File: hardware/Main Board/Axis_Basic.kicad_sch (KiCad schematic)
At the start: 63 parts, among them J1 USB4105-GF-A, J2 JST_PH, J3 JST_PH, J4 S2B-PH-K-S, J5 1175-1628-ND, J6 1-84952-4, SW1 RKB2SJK, SW2 RKB2SJK, U1 TLV493D, U2 UA78M33CDCYR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

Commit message: missed connections
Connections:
- net User_Input: now also U3.32 (PA15)
- no-connect marks 22 -> 21
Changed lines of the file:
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@@
-	)
-	(no_connect
-		(at 140.335 126.365)
 	)
 	(no_connect
@@
 			(effects
 				(font
+					(size 1.27 1.27)
+				)
+				(justify left)
+				(hide yes)
+			)
+		)
+	)
+	(global_label "User_Input"
+		(shape input)
+		(at 140.335 126.365 0)
+		(fields_autoplaced yes)
+		(effects
+			(font
+				(size 1.27 1.27)
+			)
+			(justify left)
+		)
+		(property "Intersheetrefs" "${INTERSHEET_REFS}"
+			(at 153.2987 126.365 0)
+			(effects
+				(font

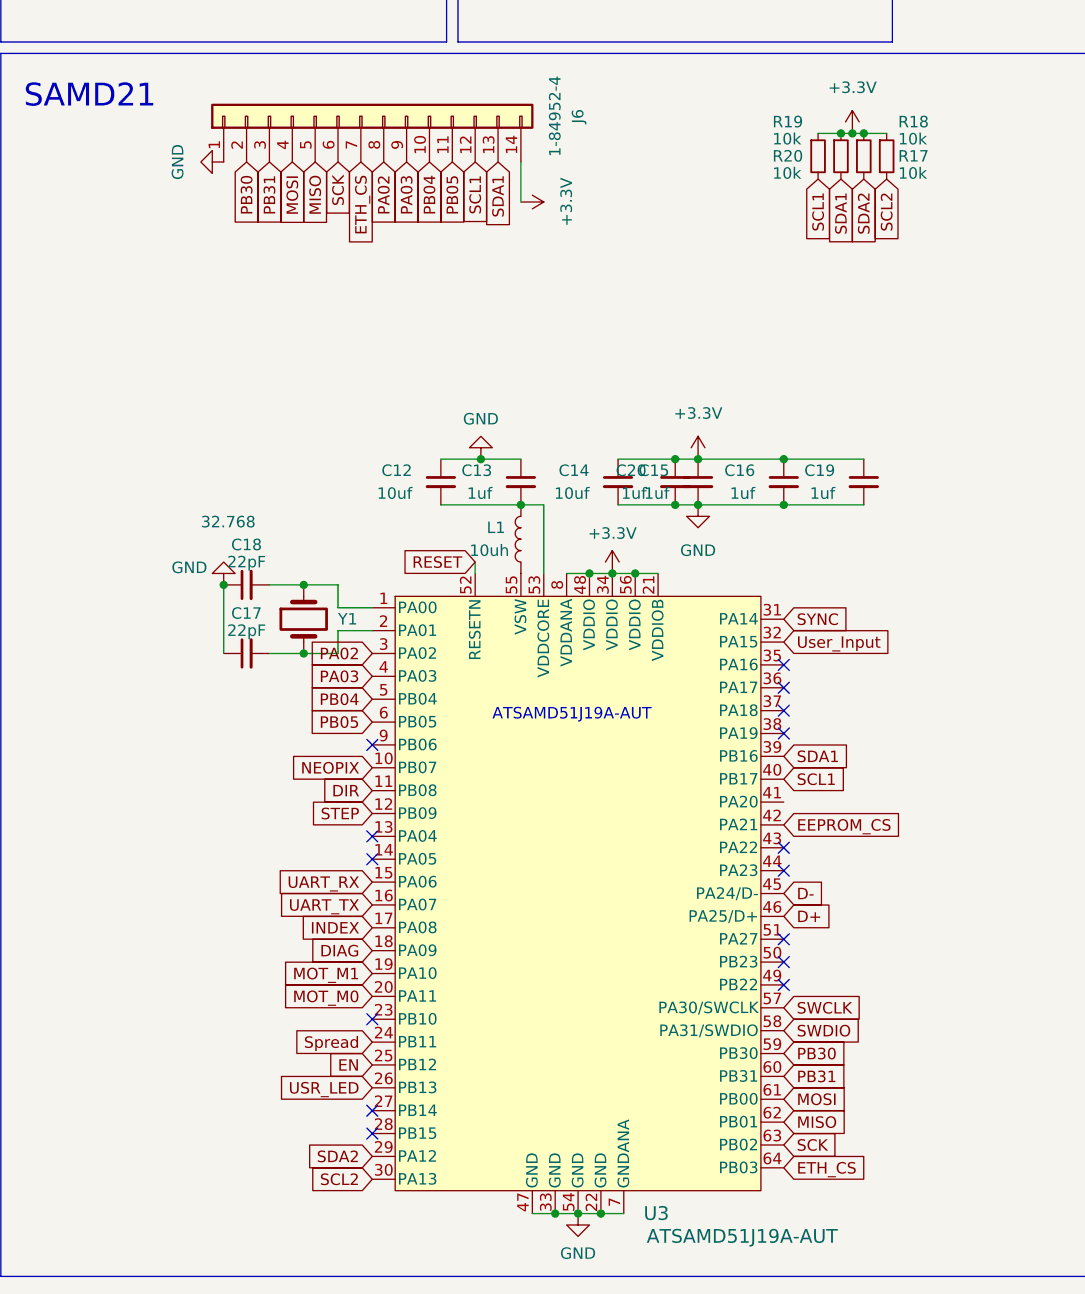
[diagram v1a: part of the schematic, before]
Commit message: Move pins for addressable LED
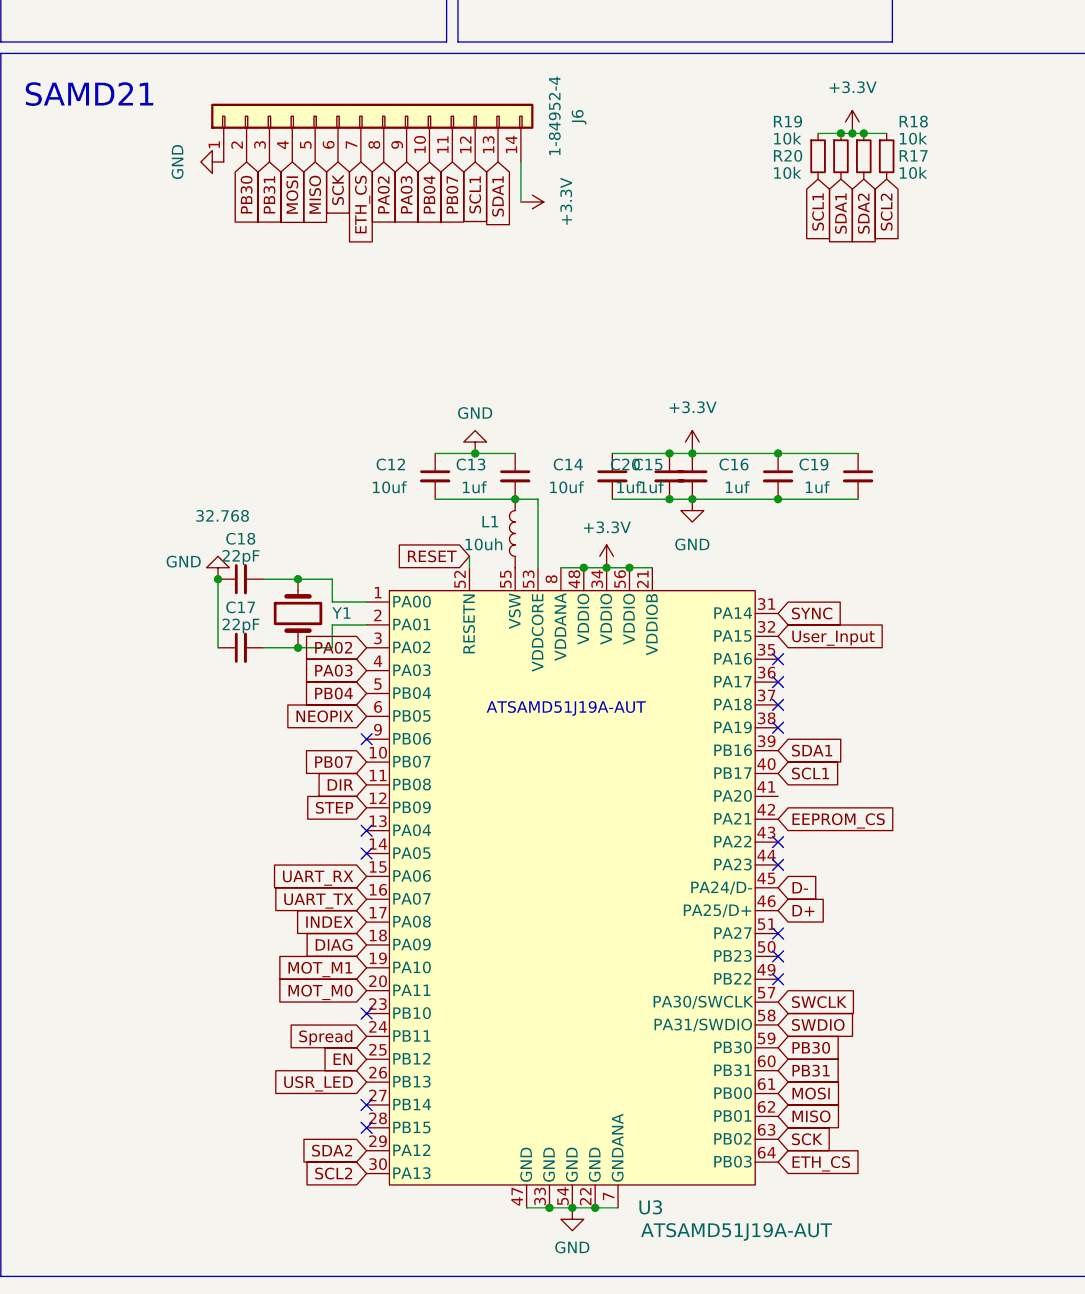
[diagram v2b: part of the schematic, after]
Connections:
- net NEOPIX: now also U3.6 (PB05); no longer U3.10 (PB07)
- net PB05 renamed PB07
- net PB07: now also U3.10 (PB07); no longer U3.6 (PB05)
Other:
- moved on the sheet: C12, C13, C14, C15, C16, C17, C18, C19, C20, L1, U3, Y1

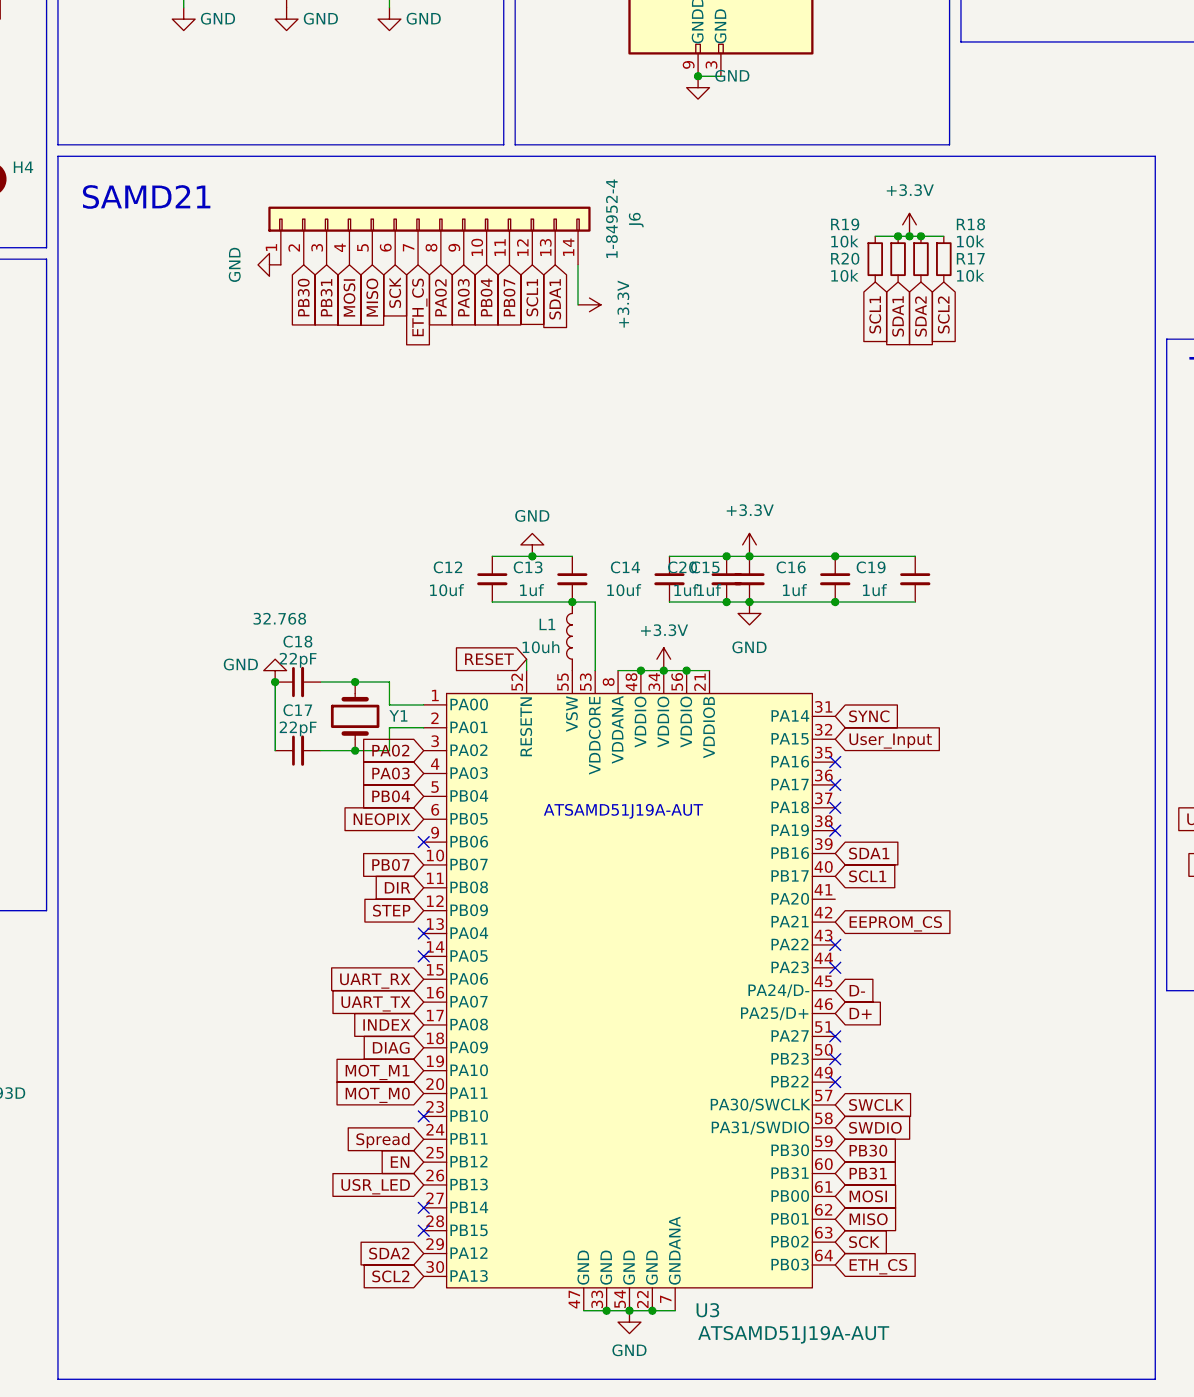
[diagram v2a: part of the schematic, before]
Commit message: Update SERCOM pins
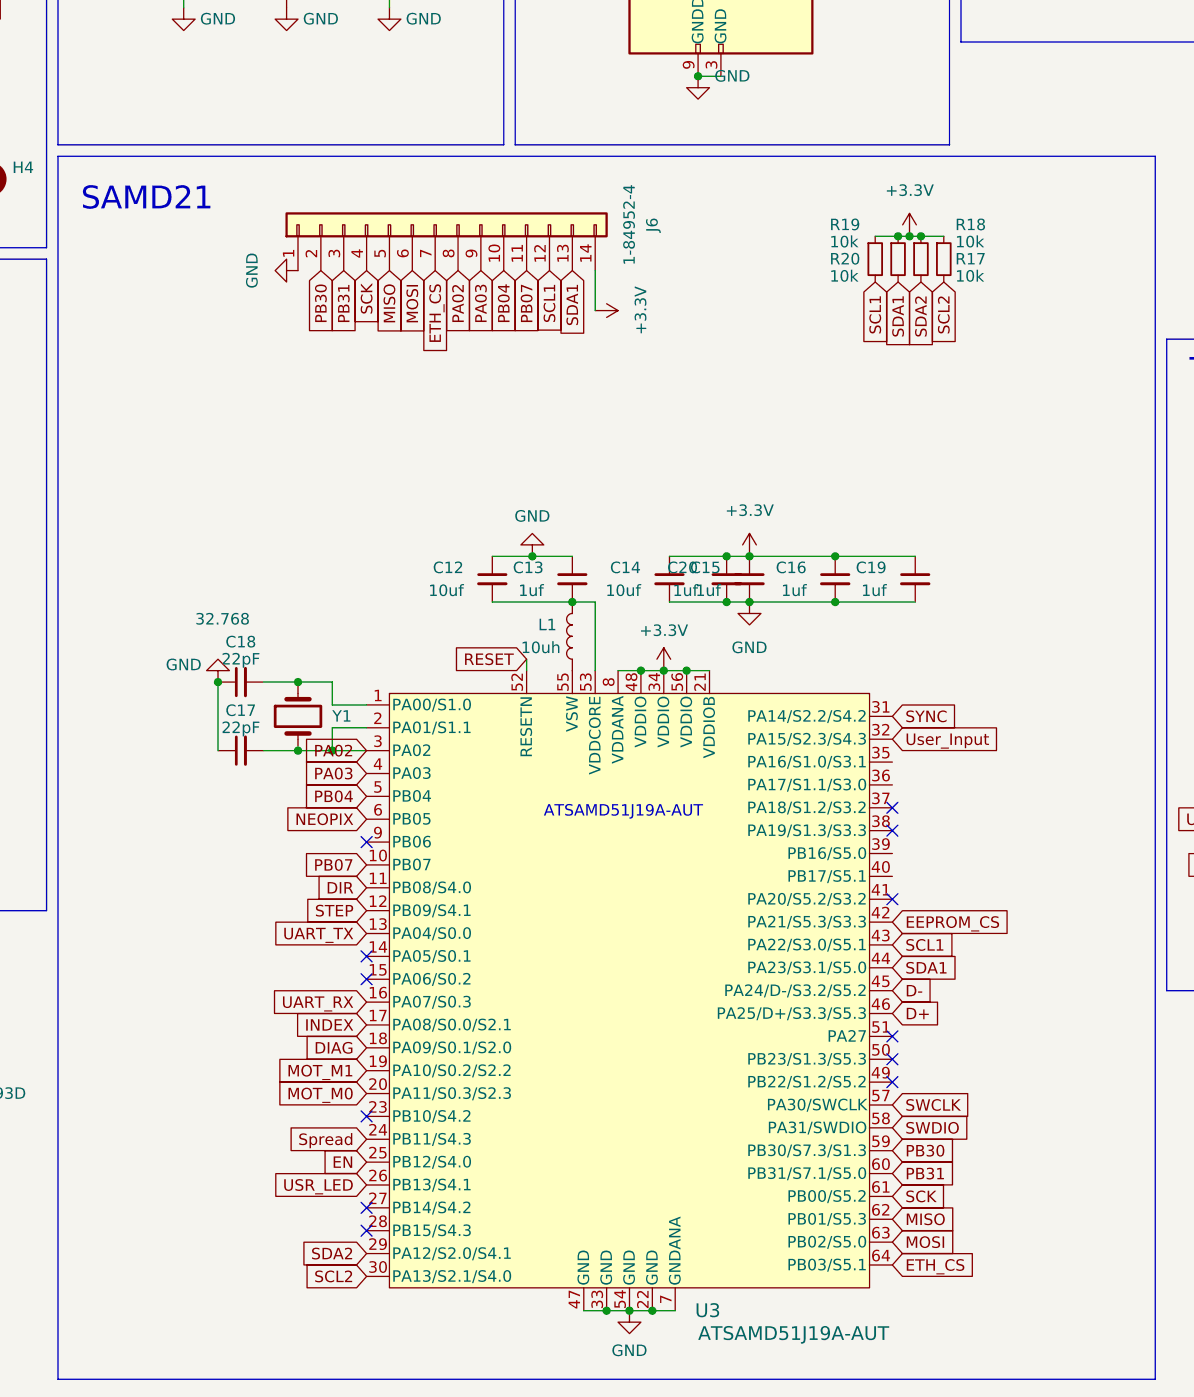
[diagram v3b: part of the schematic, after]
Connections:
- net MOSI: now also J6.6 (Pin_6), U3.63 (PB02/S5.0); no longer J6.4 (Pin_4), U3.61 (PB00)
- net PA02: now also C17.2, U3.2 (PA01/S1.1), Y1.2
- net SCK: now also J6.4 (Pin_4), U3.61 (PB00/S5.2); no longer J6.6 (Pin_6), U3.63 (PB02)
- net SCL1: now also U3.43 (PA22/S3.0/S5.1); no longer U3.40 (PB17)
- net SDA1: now also U3.44 (PA23/S3.1/S5.0); no longer U3.39 (PB16)
- net UART_RX: now also U3.16 (PA07/S0.3); no longer U3.15 (PA06)
- net UART_TX: now also U3.13 (PA04/S0.0); no longer U3.16 (PA07)
- no-connect marks 21 -> 18
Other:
- moved on the sheet: C17, C18, J6, Y1

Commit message: PCB V1.0.0 Ordered
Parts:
- removed J5: 1175-1628-ND, JTAH:JTAG_Shielded, symbol USB_C_Full_Featured:Conn_ARM_JTAG_SWD_10
- added D10, D4, D6, D8, D9: ESD5Z3V3, Diode_SMD:D_SOD-523, symbol Device:D_TVS
- added D3: MMSZ5254B, Diode_SMD:D_SOD-123, symbol Device:D_Zener
- added J5: JST_SH, Connector_JST:JST_SH_SM04B-SRSS-TB_1x04-1MP_P1.00mm_Horizontal, symbol JST:JST_PH_4pin
- added R21, R23, R24: 10k, Resistor_SMD:R_0402_1005Metric, symbol Device:R_Small
- added R22: 100k, Resistor_SMD:R_0402_1005Metric, symbol Device:R_Small
- added TP1, TP2, TP3, TP4, TP5: TestPoint, TestPoint:TestPoint_Pad_D2.0mm, symbol Connector:TestPoint
- H1, H2, H3, H4: footprint MountingHole:MountingHole_3.2mm_M3 -> MountingHole:MountingHole_3.2mm_M3_ISO14580_Pad
- J3: value JST_PH -> JST_SH; footprint Connector_JST:JST_PH_S4B-PH-K_1x04_P2.00mm_Horizontal -> Connector_JST:JST_SH_SM04B-SRSS-TB_1x04-1MP_P1.00mm_Horizontal
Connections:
- net +3.3V: now also U2.3 (VO), TP1.1; no longer U2.2 (VO)
- net D+: now also D10.1 (A1)
- net D-: now also D9.1 (A1)
- net ETH_CS: now also J6.5 (Pin_5), U3.62 (PB01/S5.3); no longer J6.7 (Pin_7), U3.64 (PB03/S5.1)
- net GND: now also J3.1, U2.2 (GND), D10.2 (A2), D3.2 (A), D4.2 (A2), D6.2 (A2), D8.2 (A2), D9.2 (A2), J5.1, R21.2, R24.2, TP2.1; no longer J3.4, U2.1 (GND)
- net MISO: now also J6.4 (Pin_4), U3.61 (PB00/S5.2); no longer J6.5 (Pin_5), U3.62 (PB01/S5.3)
- net RESET: now also TP5.1
- net SCK: now also J6.7 (Pin_7), U3.64 (PB03/S5.1); no longer J6.4 (Pin_4), U3.61 (PB00/S5.2)
- net SCL2: now also J3.4, D6.1 (A1), J5.4; no longer J3.1
- net SDA2: now also J3.3, D4.1 (A1), J5.3; no longer J3.2
- net SWCLK: now also TP4.1
- net SWDIO: now also TP3.1
- net SYNC: now also J3.2, D8.1 (A1), J5.2; no longer J3.3
- net VCC: now also U2.1 (VI), D3.1 (K), R22.1; no longer U2.3 (VI)
- net V_USB: now also R23.1
- net VUSB_sense: now reaches U3.15 (PA06/S0.2)
- net VUSB_sense: now also R23.2, R24.1
- net V_sense: now reaches U3.9 (PB06)
- net V_sense: now also R21.1, R22.2
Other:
- note added: "S0: UART"
- note added: "S2: I2C_2"
- note added: "S3: I2C_1"
- note added: "S5: SPI"
- moved on the sheet: C2, R4, U2

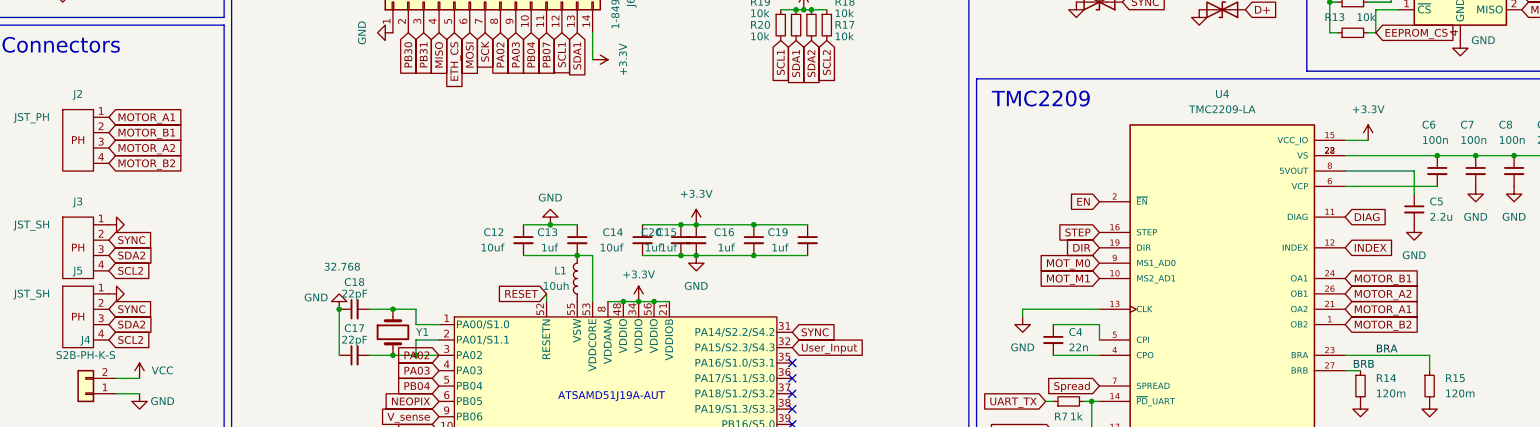
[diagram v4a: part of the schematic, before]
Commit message: Correct motor phase naming
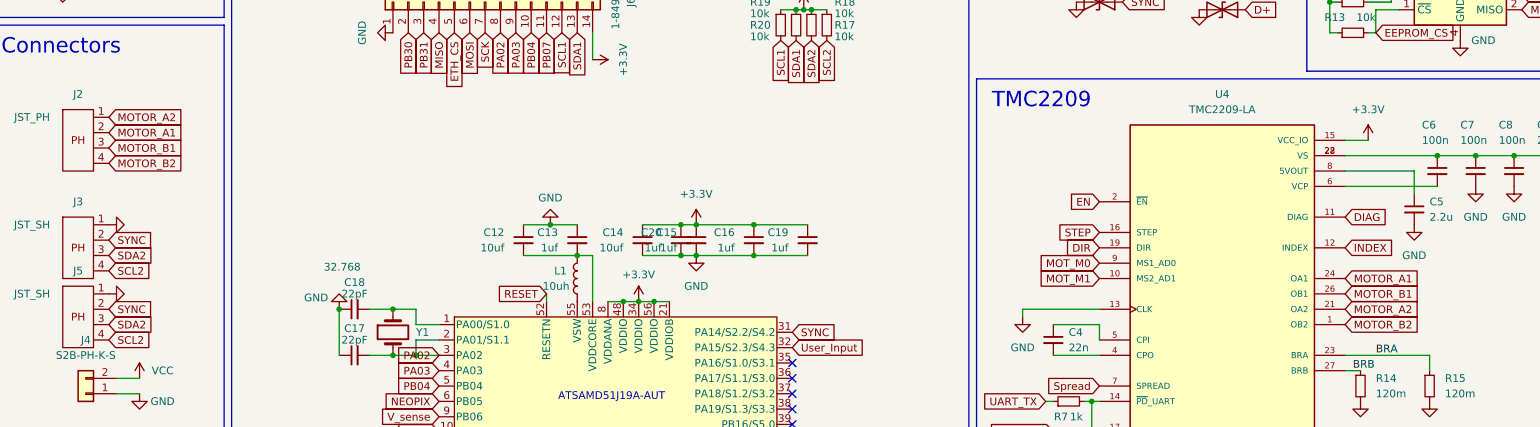
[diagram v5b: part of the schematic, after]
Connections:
- net MOTOR_A1: now also J2.2, U4.24 (OA1); no longer J2.1, U4.21 (OA2)
- net MOTOR_A2: now also J2.1, U4.21 (OA2); no longer J2.3, U4.26 (OB1)
- net MOTOR_B1: now also J2.3, U4.26 (OB1); no longer J2.2, U4.24 (OA1)
